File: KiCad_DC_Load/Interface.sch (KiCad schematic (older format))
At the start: 0 parts

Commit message: Power supply and connectors
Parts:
- added Display_I2C: Conn_01x04, symbol Connector_Generic:Conn_01x04
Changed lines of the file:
@@
 Comment4 "HappyDonuts"
 $EndDescr
+$Comp
+L Connector_Generic:Conn_01x04 Display_I2C
+U 1 1 60C188AF
+P 2100 1650
+F 0 "Display_I2C" H 2180 1642 50  0000 L CNN
+F 1 "Conn_01x04" H 2180 1551 50  0000 L CNN
+F 2 "" H 2100 1650 50  0001 C CNN
+F 3 "~" H 2100 1650 50  0001 C CNN
+	1    2100 1650
+	1    0    0    -1
+$EndComp
 $EndSCHEMATC

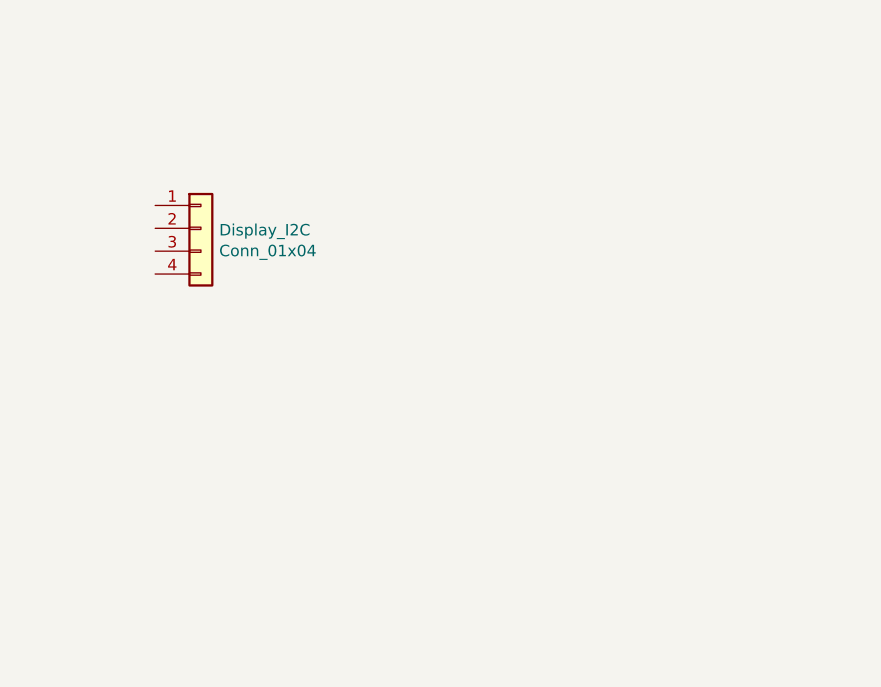
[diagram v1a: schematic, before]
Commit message: Interface added
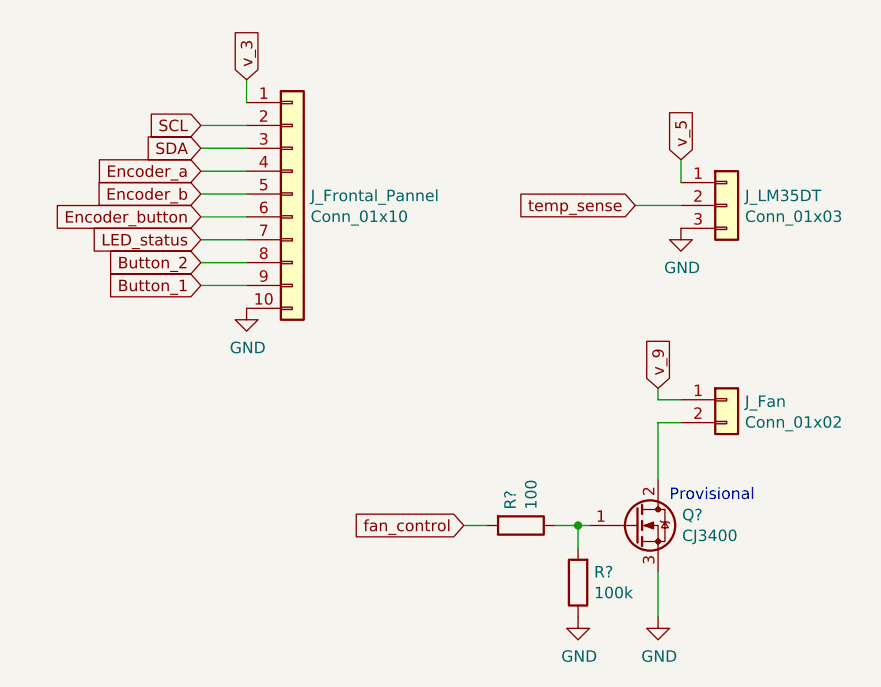
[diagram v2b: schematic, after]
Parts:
- removed Display_I2C: Conn_01x04, symbol Connector_Generic:Conn_01x04
- added J_Fan: Conn_01x02, symbol Connector_Generic:Conn_01x02
- added J_Frontal_Pannel: Conn_01x10, symbol Connector_Generic:Conn_01x10
- added J_LM35DT: Conn_01x03, symbol Connector_Generic:Conn_01x03
- added Q?: CJ3400, symbol Device:Q_NMOS_GDS
- added R?: 100k, symbol Device:R
- added R?: 100, symbol Device:R
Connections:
- new net: J_Fan.2 (Pin_2), Q?.2 (D)
- new net: Q?.1 (G), R?.1, R?.2
- new net Button_1: J_Frontal_Pannel.9 (Pin_9)
- new net Button_2: J_Frontal_Pannel.8 (Pin_8)
- new net Encoder_a: J_Frontal_Pannel.4 (Pin_4)
- new net Encoder_b: J_Frontal_Pannel.5 (Pin_5)
- new net Encoder_button: J_Frontal_Pannel.6 (Pin_6)
- new net GND: J_Frontal_Pannel.10 (Pin_10), J_LM35DT.3 (Pin_3), Q?.3 (S), R?.1
- new net LED_status: J_Frontal_Pannel.7 (Pin_7)
- new net SCL: J_Frontal_Pannel.2 (Pin_2)
- new net SDA: J_Frontal_Pannel.3 (Pin_3)
- new net fan_control: R?.2
- new net temp_sense: J_LM35DT.2 (Pin_2)
- new net v_3: J_Frontal_Pannel.1 (Pin_1)
- new net v_5: J_LM35DT.1 (Pin_1)
- new net v_9: J_Fan.1 (Pin_1)
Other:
- note added: "Provisional"
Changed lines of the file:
@@
 $EndDescr
 $Comp
-L Connector_Generic:Conn_01x04 Display_I2C
-U 1 1 60C188AF
-P 2100 1650
-F 0 "Display_I2C" H 2180 1642 50  0000 L CNN
-F 1 "Conn_01x04" H 2180 1551 50  0000 L CNN
-F 2 "" H 2100 1650 50  0001 C CNN
-F 3 "~" H 2100 1650 50  0001 C CNN
-	1    2100 1650
+L Connector_Generic:Conn_01x10 J_Frontal_Pannel
+U 1 1 60C34992
+P 2500 1500
+F 0 "J_Frontal_Pannel" H 2580 1492 50  0000 L CNN
+F 1 "Conn_01x10" H 2580 1401 50  0000 L CNN
+F 2 "" H 2500 1500 50  0001 C CNN
+F 3 "~" H 2500 1500 50  0001 C CNN
+	1    2500 1500
 	1    0    0    -1
 $EndComp
+$Comp
+L Connector_Generic:Conn_01x03 J_LM35DT
+U 1 1 60C36774
+P 4400 1550
+F 0 "J_LM35DT" H 4480 1592 50  0000 L CNN
+F 1 "Conn_01x03" H 4480 1501 50  0000 L CNN
+F 2 "" H 4400 1550 50  0001 C CNN
+F 3 "~" H 4400 1550 50  0001 C CNN
+	1    4400 1550
+	1    0    0    -1
+$EndComp
+$Comp
+L Connector_Generic:Conn_01x02 J_Fan
+U 1 1 60C371EC
+P 4400 2400
+F 0 "J_Fan" H 4480 2392 50  0000 L CNN
+F 1 "Conn_01x02" H 4480 2301 50  0000 L CNN
+F 2 "" H 4400 2400 50  0001 C CNN
+F 3 "~" H 4400 2400 50  0001 C CNN
+	1    4400 2400
+	1    0    0    -1
+$EndComp
+Wire Wire Line
+	4100 2500 4100 2750
+$Comp
+L power:GND #PWR?
+U 1 1 60C5EBB3
+P 4100 3350
+AR Path="/5FD0FB16/60C5EBB3" Ref="#PWR?"  Part="1"
+AR Path="/5FD0FFBC/60C5EBB3" Ref="#PWR?"  Part="1"
+F 0 "#PWR?" H 4100 3100 50  0001 C CNN
+F 1 "GND" H 4105 3177 50  0000 C CNN
+F 2 "" H 4100 3350 50  0001 C CNN
+F 3 "" H 4100 3350 50  0001 C CNN
+	1    4100 3350
+	1    0    0    -1
+$EndComp
+$Comp
+L Device:R R?
+U 1 1 60C5EBB9
+P 3750 3200
+AR Path="/5FD0FB16/60C5EBB9" Ref="R?"  Part="1"
+AR Path="/5FD0FFBC/60C5EBB9" Ref="R?"  Part="1"
+F 0 "R?" H 3680 3154 50  0000 R CNN
+F 1 "100k" H 3680 3245 50  0000 R CNN
+F 2 "" V 3680 3200 50  0001 C CNN
+F 3 "~" H 3750 3200 50  0001 C CNN
+	1    3750 3200
+	-1   0    0    1
+$EndComp
+Wire Wire Line
+	3750 3050 3750 2950
+Wire Wire Line
+	3750 2950 3800 2950
+$Comp
+L power:GND #PWR?
+U 1 1 60C5EBC1
+P 3750 3350
+AR Path="/5FD0FB16/60C5EBC1" Ref="#PWR?"  Part="1"
+AR Path="/5FD0FFBC/60C5EBC1" Ref="#PWR?"  Part="1"
+F 0 "#PWR?" H 3750 3100 50  0001 C CNN
+F 1 "GND" H 3755 3177 50  0000 C CNN
+F 2 "" H 3750 3350 50  0001 C CNN
+F 3 "" H 3750 3350 50  0001 C CNN
+	1    3750 3350
+	1    0    0    -1
+$EndComp
+Wire Wire Line
+	4100 3150 4100 3350
+Text GLabel 3250 2950 0    50   Input ~ 0
+fan_control
+$Comp
+L Device:R R?
+U 1 1 60C5EBC9
+P 3500 2950
+AR Path="/5FD0FB16/60C5EBC9" Ref="R?"  Part="1"
+AR Path="/5FD0FFBC/60C5EBC9" Ref="R?"  Part="1"
+F 0 "R?" H 3430 2904 50  0000 R CNN
+F 1 "100" H 3430 2995 50  0000 R CNN
+F 2 "" V 3430 2950 50  0001 C CNN
+F 3 "~" H 3500 2950 50  0001 C CNN
+	1    3500 2950
+	0    1    1    0
+$EndComp
+Wire Wire Line
+	3750 2950 3650 2950
+Connection ~ 3750 2950
+Wire Wire Line
+	3350 2950 3250 2950
+Wire Wire Line
+	4100 2500 4200 2500
+Text GLabel 4100 2350 1    50   Input ~ 0
+v_9
+Wire Wire Line
+	4100 2350 4100 2400
+Wire Wire Line
+	4100 2400 4200 2400
+Text Notes 4150 2850 0    50   ~ 0
+Provisional
+$Comp
+L power:GND #PWR?
+U 1 1 60C64DD4
+P 4200 1650
+AR Path="/5FD0FB16/60C64DD4" Ref="#PWR?"  Part="1"
+AR Path="/5FD0FFBC/60C64DD4" Ref="#PWR?"  Part="1"
+F 0 "#PWR?" H 4200 1400 50  0001 C CNN
+F 1 "GND" H 4205 1477 50  0000 C CNN
+F 2 "" H 4200 1650 50  0001 C CNN
+F 3 "" H 4200 1650 50  0001 C CNN
+	1    4200 1650
+	1    0    0    -1
+$EndComp
+Text GLabel 4200 1350 1    50   Input ~ 0
+v_5
+Wire Wire Line
+	4200 1450 4200 1350
+Text GLabel 4000 1550 0    50   Input ~ 0
+temp_sense
+Wire Wire Line
+	4000 1550 4200 1550
+$Comp
+L power:GND #PWR?
+U 1 1 60C65CA7
+P 2300 2000
+AR Path="/5FD0FB16/60C65CA7" Ref="#PWR?"  Part="1"
+AR Path="/5FD0FFBC/60C65CA7" Ref="#PWR?"  Part="1"
+F 0 "#PWR?" H 2300 1750 50  0001 C CNN
+F 1 "GND" H 2305 1827 50  0000 C CNN
+F 2 "" H 2300 2000 50  0001 C CNN
+F 3 "" H 2300 2000 50  0001 C CNN
+	1    2300 2000
+	1    0    0    -1
+$EndComp
+Text GLabel 2300 1000 1    50   Input ~ 0
+v_3
+Wire Wire Line
+	2300 1000 2300 1100
+Text GLabel 2100 1900 0    50   Input ~ 0
+Button_1
+Text GLabel 2100 1800 0    50   Input ~ 0
+Button_2
+Text GLabel 2100 1700 0    50   Input ~ 0
+LED_status
+Text GLabel 2100 1600 0    50   Input ~ 0
+Encoder_button
+Text GLabel 2100 1500 0    50   Input ~ 0
+Encoder_b
+Text GLabel 2100 1400 0    50   Input ~ 0
+Encoder_a
+Text GLabel 2100 1300 0    50   Input ~ 0
+SDA
+Text GLabel 2100 1200 0    50   Input ~ 0
+SCL
+Wire Wire Line
+	2100 1200 2300 1200
+Wire Wire Line
+	2100 1300 2300 1300
+Wire Wire Line
+	2100 1400 2300 1400
+Wire Wire Line
+	2100 1500 2300 1500
+Wire Wire Line
+	2100 1600 2300 1600
+Wire Wire Line
+	2100 1700 2300 1700
+Wire Wire Line
+	2100 1800 2300 1800
+Wire Wire Line
+	2100 1900 2300 1900
+$Comp
+L Device:Q_NMOS_GDS Q?
+U 1 1 60C78C77
+P 4000 2950
+AR Path="/5FD0FB16/60C78C77" Ref="Q?"  Part="1"
+AR Path="/5FD0FFBC/60C78C77" Ref="Q?"  Part="1"
+F 0 "Q?" H 4205 2996 50  0000 L CNN
+F 1 "CJ3400" H 4205 2905 50  0000 L CNN
+F 2 "" H 4200 3050 50  0001 C CNN
+F 3 "~" H 4000 2950 50  0001 C CNN
+	1    4000 2950
+	1    0    0    -1
+$EndComp
